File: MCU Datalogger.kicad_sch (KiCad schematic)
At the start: 25 parts

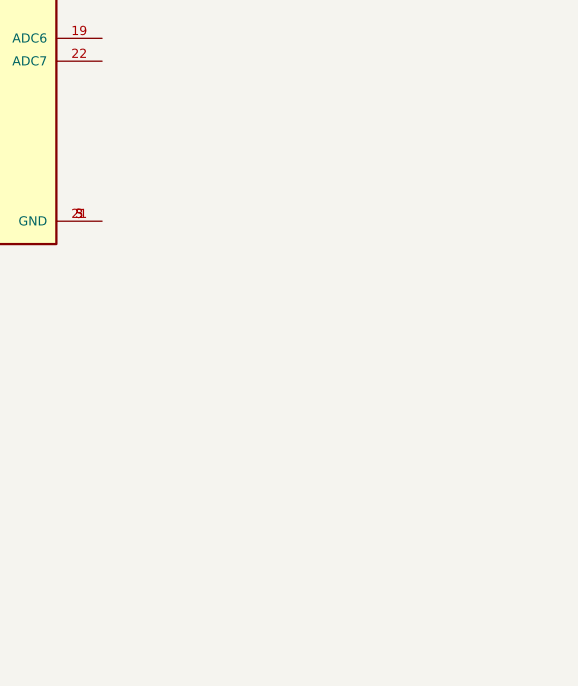
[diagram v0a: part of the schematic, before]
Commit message: Add Connectors (in subpage)
Created the sub page, added the connectors
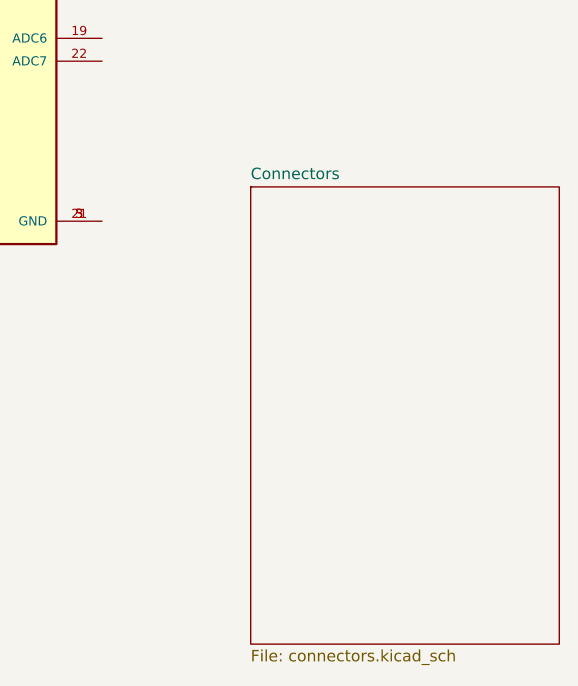
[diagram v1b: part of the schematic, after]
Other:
- added sheet Connectors (connectors.kicad_sch)
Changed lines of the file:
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@@
+    )
+  )
+  (sheet (at 130.81 109.22) (size 34.29 50.8) (fields_autoplaced)
+    (stroke (width 0.1524) (type solid) (color 0 0 0 0))
+    (fill (color 0 0 0 0.0000))
+    (property "Sheet name" "Connectors" (id 0) (at 130.81 108.5084 0)
+      (effects (font (size 1.27 1.27)) (justify left bottom))
+    )
+    (property "Sheet file" "connectors.kicad_sch" (id 1) (at 130.81 160.6046 0)
+      (effects (font (size 1.27 1.27)) (justify left top))
     )
   )
   (sheet_instances
     (path "/" (page "1"))
+    (path "/f4442191-4550-4891-b6d8-ca11a3d77e6c" (page "2"))
   )
   (symbol_instances
@@
       (reference "H?") (unit 1) (value "MountingHole") (footprint "")
     )
+    (path "/f4442191-4550-4891-b6d8-ca11a3d77e6c/bdb029af-1da8-4b14-94e8-abe7e35af1cc"
+      (reference "J?") (unit 1) (value "Conn_02x03_Odd_Even") (footprint "")
+    )
+    (path "/f4442191-4550-4891-b6d8-ca11a3d77e6c/d7b71f2c-04c1-4709-9591-080d8cb9e557"
+      (reference "J?") (unit 1) (value "Conn_01x04_Male") (footprint "")
+    )
+    (path "/f4442191-4550-4891-b6d8-ca11a3d77e6c/f7ce2f65-abc3-46a7-b3bd-15180bb27308"
+      (reference "J?") (unit 1) (value "Conn_01x09_Male") (footprint "")
+    )
+    (path "/f4442191-4550-4891-b6d8-ca11a3d77e6c/fb02a4cf-7ac5-4a81-8ef5-af57cfa1f15a"
+      (reference "J?") (unit 1) (value "Conn_01x04_Male") (footprint "")
+    )
     (path "/21a1c133-f7c0-4c55-bfae-87489f29c903"

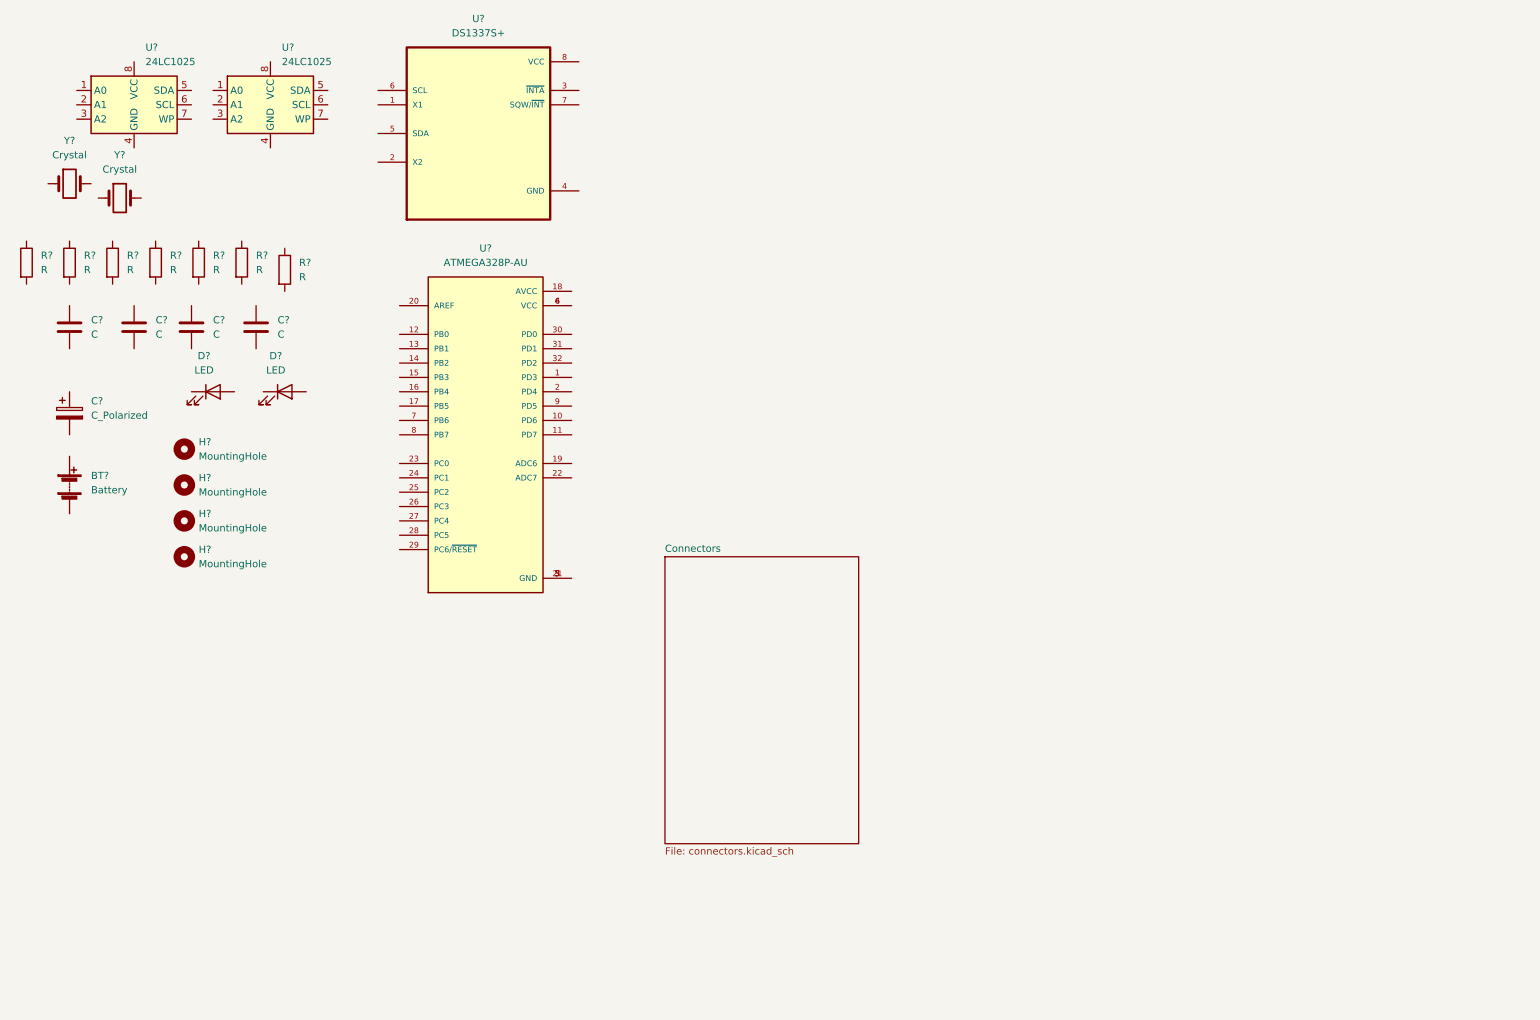
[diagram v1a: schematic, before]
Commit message: Arranged and annotated the symbols
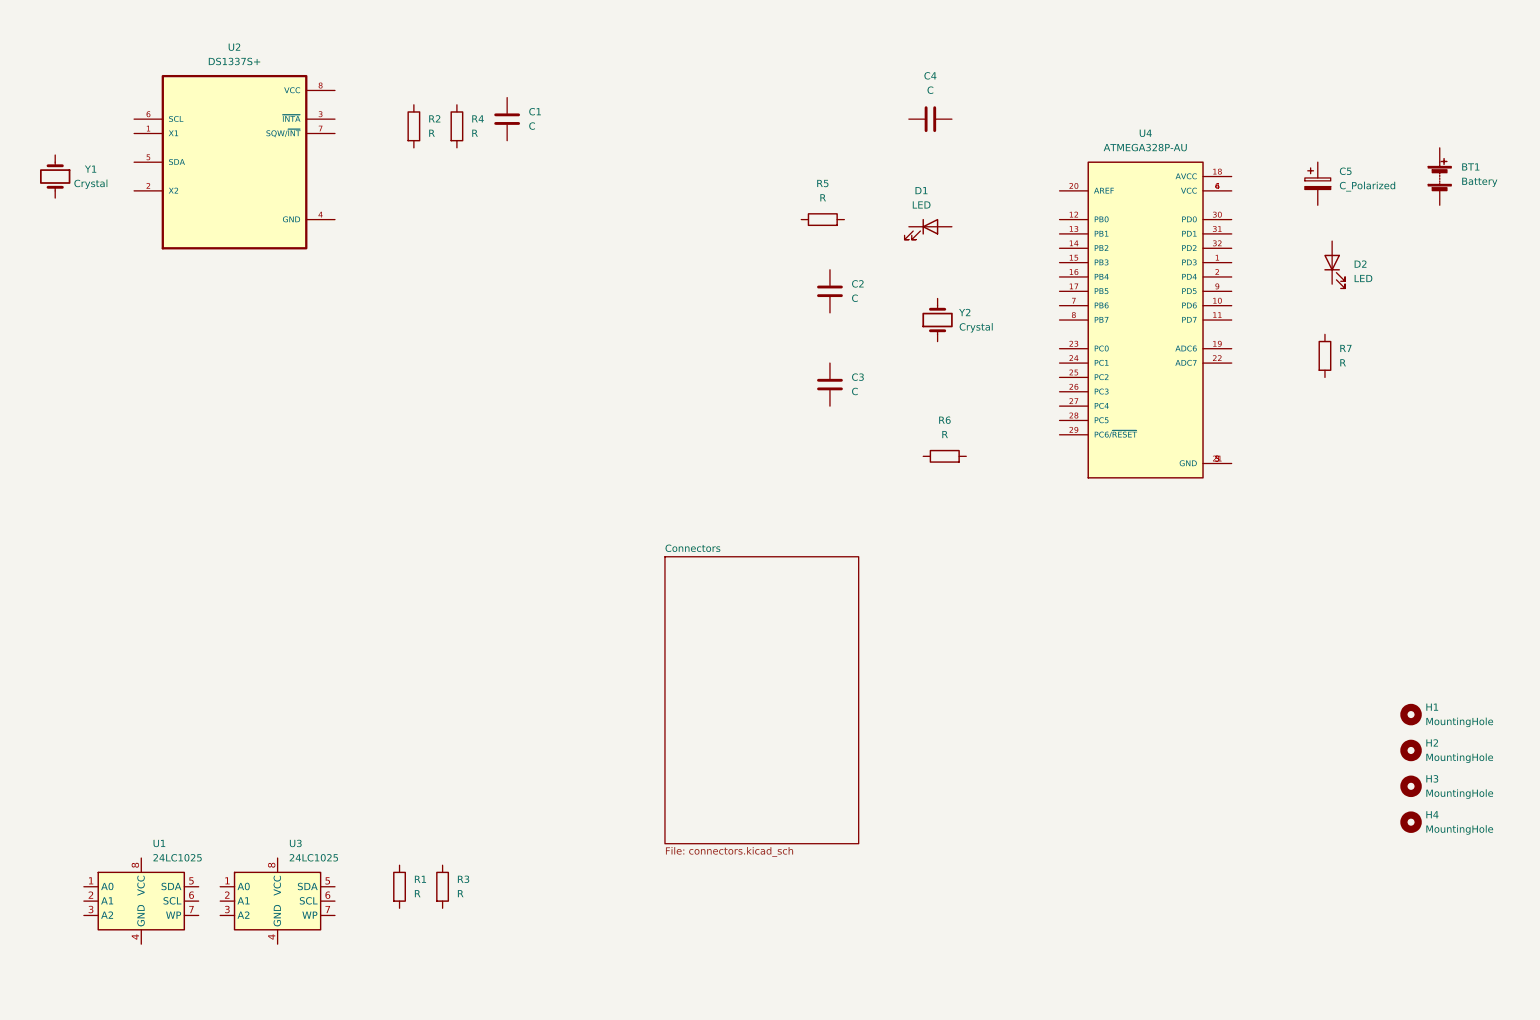
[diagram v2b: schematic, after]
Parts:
- gave numbers to parts that had none: 25
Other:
- moved on the sheet: BT1, C1, C2, C3, C4, C5, D1, D2, H1, H2, H3, H4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

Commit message: set values on the relevant symbols
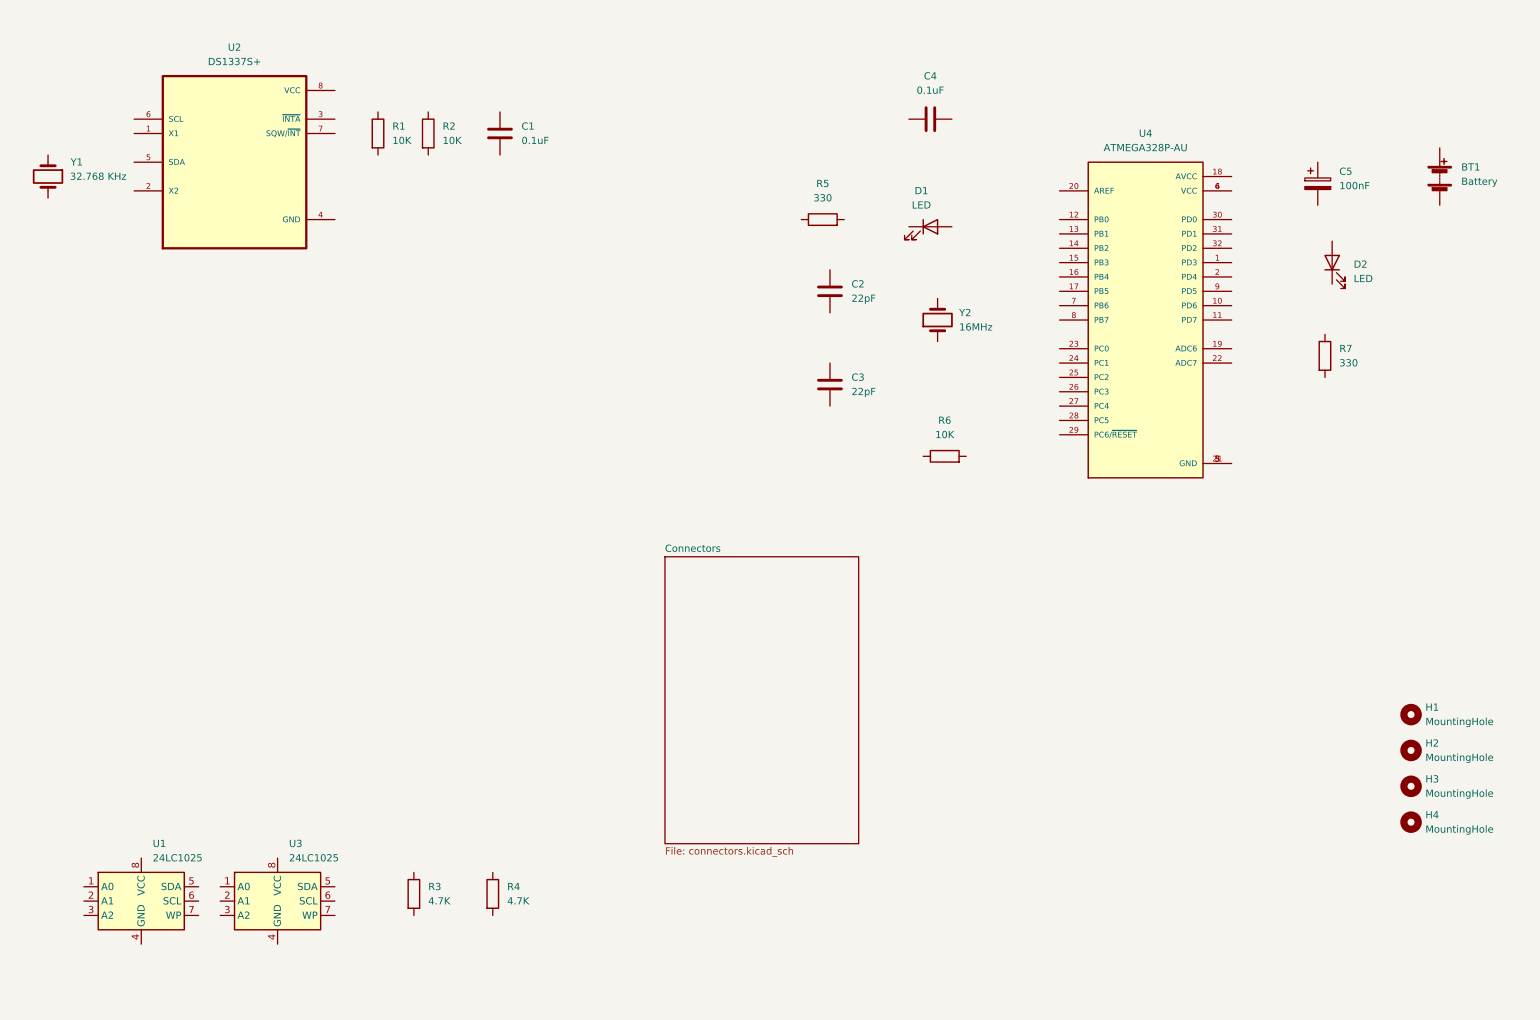
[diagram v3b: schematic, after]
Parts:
- C1, C4: value C -> 0.1uF
- C2, C3: value C -> 22pF
- C5: value C_Polarized -> 100nF
- R1, R2, R6: value R -> 10K
- R3, R4: value R -> 4.7K
- R5, R7: value R -> 330
- Y1: value Crystal -> 32.768 KHz
- Y2: value Crystal -> 16MHz
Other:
- moved on the sheet: C1, R1, R2, R3, R4, Y1

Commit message: Import footprints. Associated the symbols to the footprints I want to use
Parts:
- BT1: footprint (none) -> Connector_PinHeader_2.54mm:PinHeader_1x02_P2.54mm_Vertical
- C1, C2, C3, C4, C5: footprint (none) -> Capacitor_SMD:C_0805_2012Metric
- D1, D2: footprint (none) -> LED_SMD:LED_0805_2012Metric
- H1, H2, H3, H4: footprint (none) -> MountingHole:MountingHole_2.1mm
- R1, R2, R3, R4, R5, R6, R7: footprint (none) -> Resistor_SMD:R_0805_2012Metric
- U1, U3: footprint (none) -> Package_SO:SOIC-8_5.23x5.23mm_P1.27mm
- U2: footprint SOIC127P600X175-8N -> Footprints:SOIC127P600X175-8N
- U4: footprint QFP80P900X900X120-32N -> Footprints:QFP80P900X900X120-32N
- Y1, Y2: footprint (none) -> Crystal:Crystal_SMD_5032-2Pin_5.0x3.2mm_HandSoldering

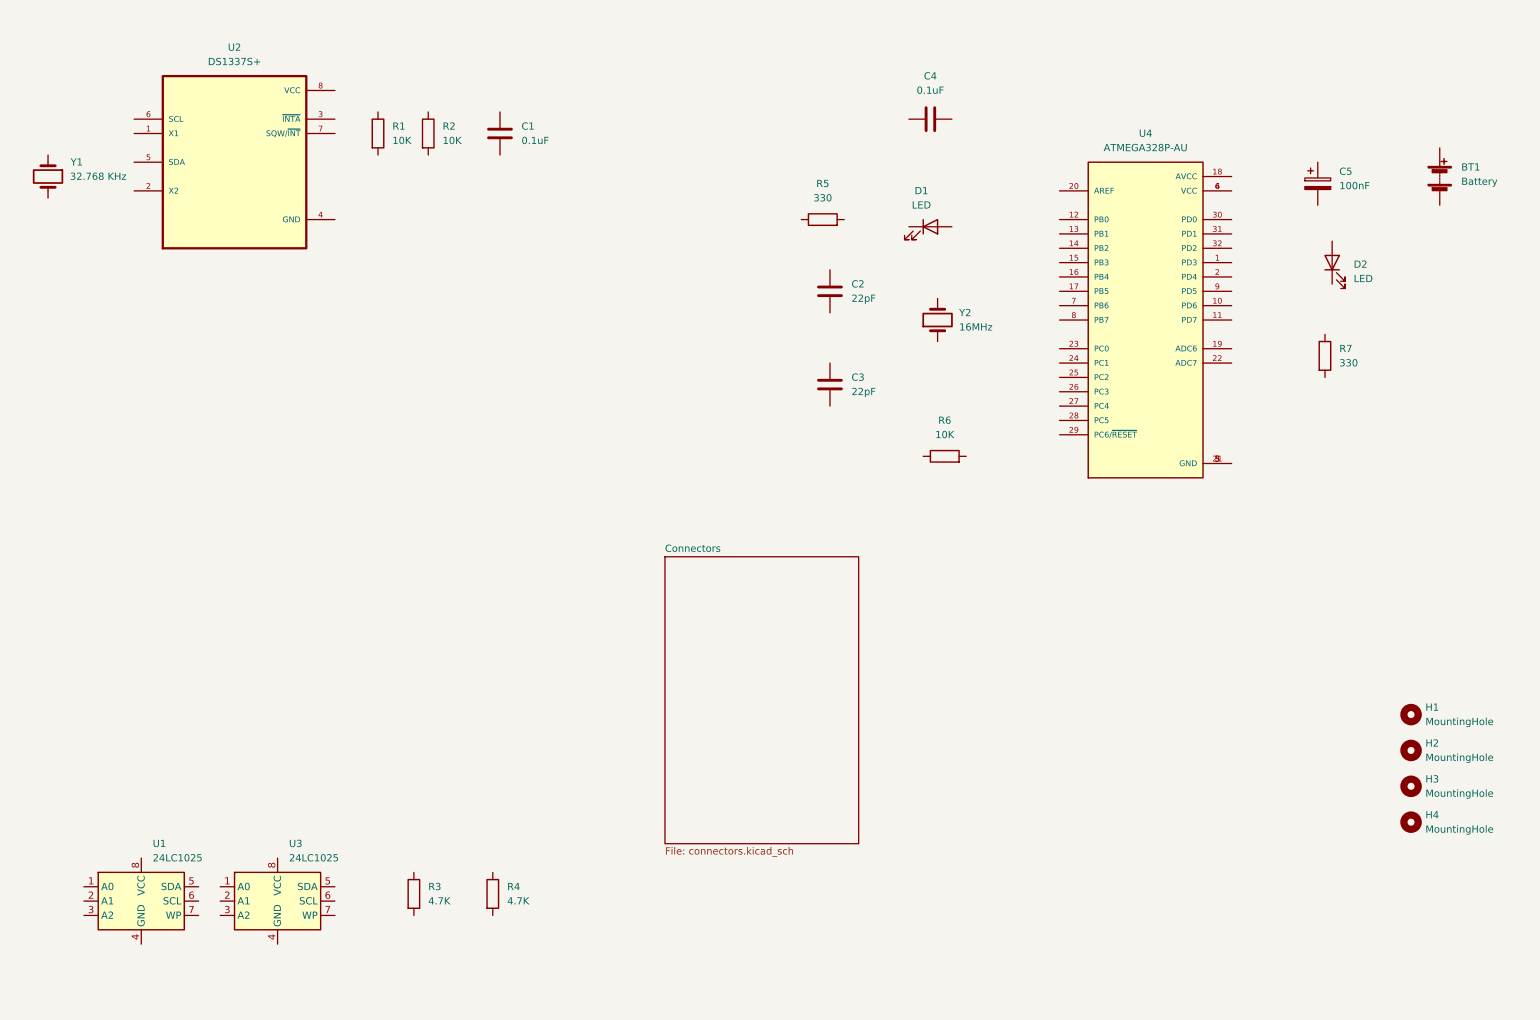
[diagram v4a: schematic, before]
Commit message: Part of the wiring done. On the main sheet. Still need to add some labels
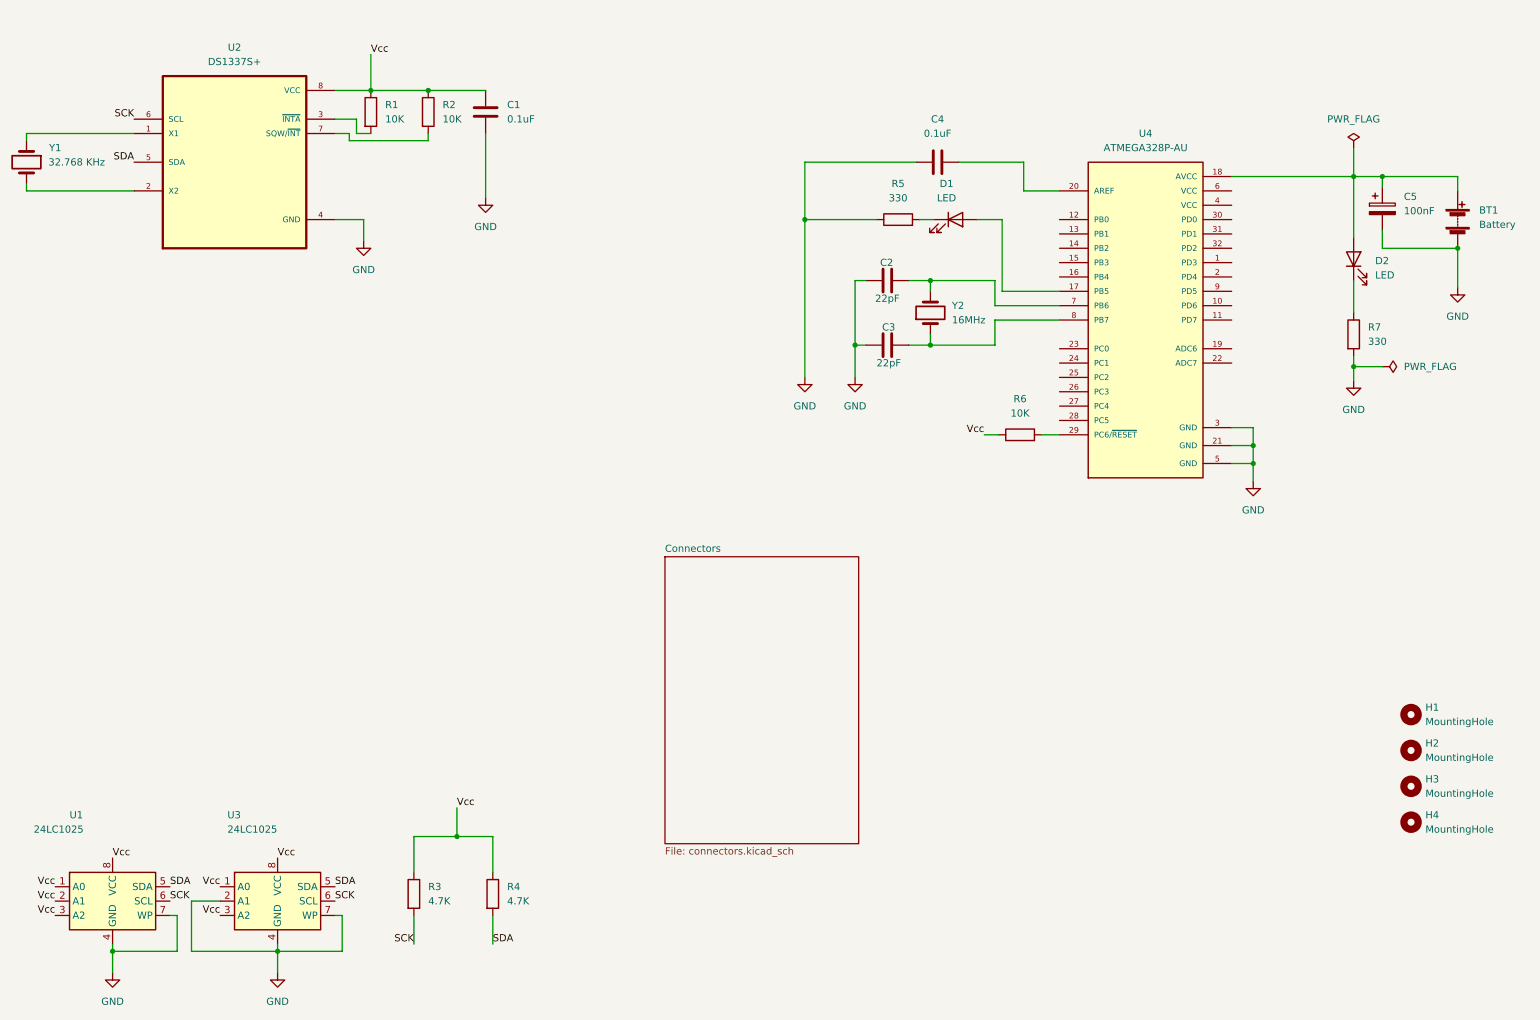
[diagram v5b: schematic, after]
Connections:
- net at Y2.1: now also C3.2, U4.8 (PB7)
- net at Y2.2: now also C2.2, U4.7 (PB6)
- net GND: now reaches C2.1
- net GND: now also BT1.2 (-), C1.2, C3.1, C4.1, C5.2, R5.1, R7.2, U1.4 (GND), U1.7 (WP), U2.4 (GND), U3.2 (A1), U3.4 (GND), U3.7 (WP), U4.21 (GND), U4.3 (GND), U4.5 (GND)
- net Vcc: now reaches R3.1
- net Vcc: now also C1.1, R1.1, R2.1, R4.1, R6.1, U1.1 (A0), U1.2 (A1), U1.3 (A2), U1.8 (VCC), U2.8 (VCC), U3.1 (A0), U3.3 (A2), U3.8 (VCC)
- net SCK: now reaches R3.2
- net SCK: now also U1.6 (SCL), U2.6 (SCL), U3.6 (SCL)
- net SDA: now reaches U1.5 (SDA)
- net SDA: now also R4.2, U2.5 (SDA), U3.5 (SDA)
- net at R2.2: now also U2.7 (SQW/~{INT})
- net at C4.2: now also U4.20 (AREF)
- net at R5.2: now also D1.1 (K)
- net at R1.2: now also U2.3 (~{INTA})
- net at D1.2 (A): now also U4.17 (PB5)
- net at D2.1 (K): now also R7.1
- net at D2.2 (A): now also BT1.1 (+), C5.1, U4.18 (AVCC)
- net at U4.29 (PC6/~{RESET}): now also R6.2
- net at U4.4 (VCC): no longer U4.6 (VCC)
- net at Y1.1: now also U2.1 (X1)
- net at Y1.2: now also U2.2 (X2)
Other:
- moved on the sheet: BT1, C1, C2, C3, C4, C5, D1, D2, R1, R2, R5, R6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
